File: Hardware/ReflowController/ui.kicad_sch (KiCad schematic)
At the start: 1 part, among them U8 PI4IOE5V6416

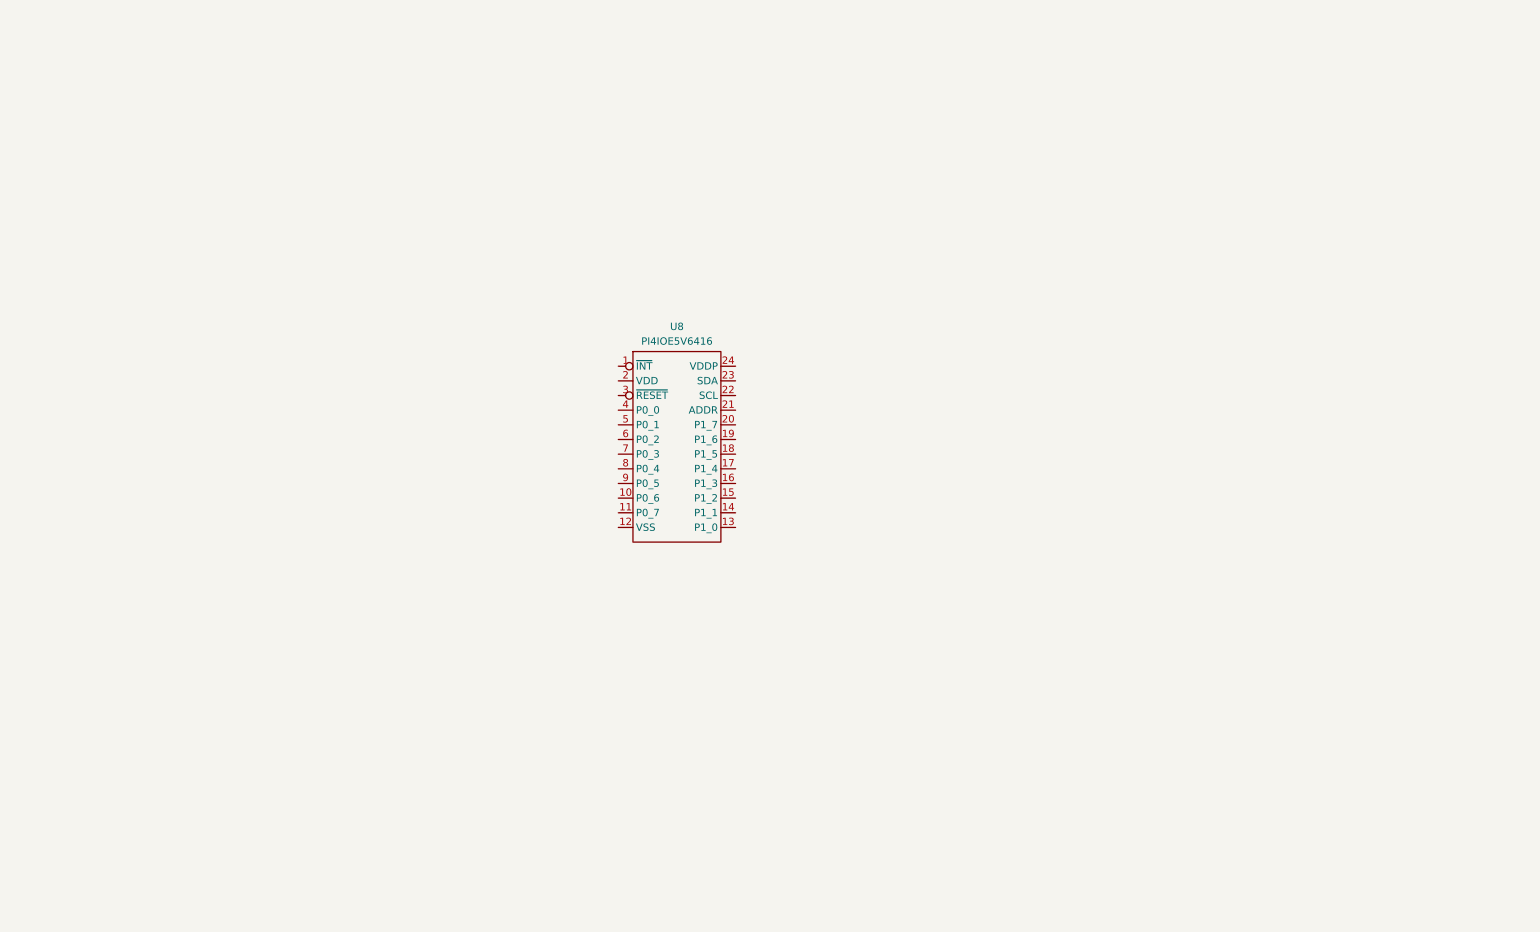
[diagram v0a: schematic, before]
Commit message: added the schematic of the updated pwerAndUi branch(with uC schematic update
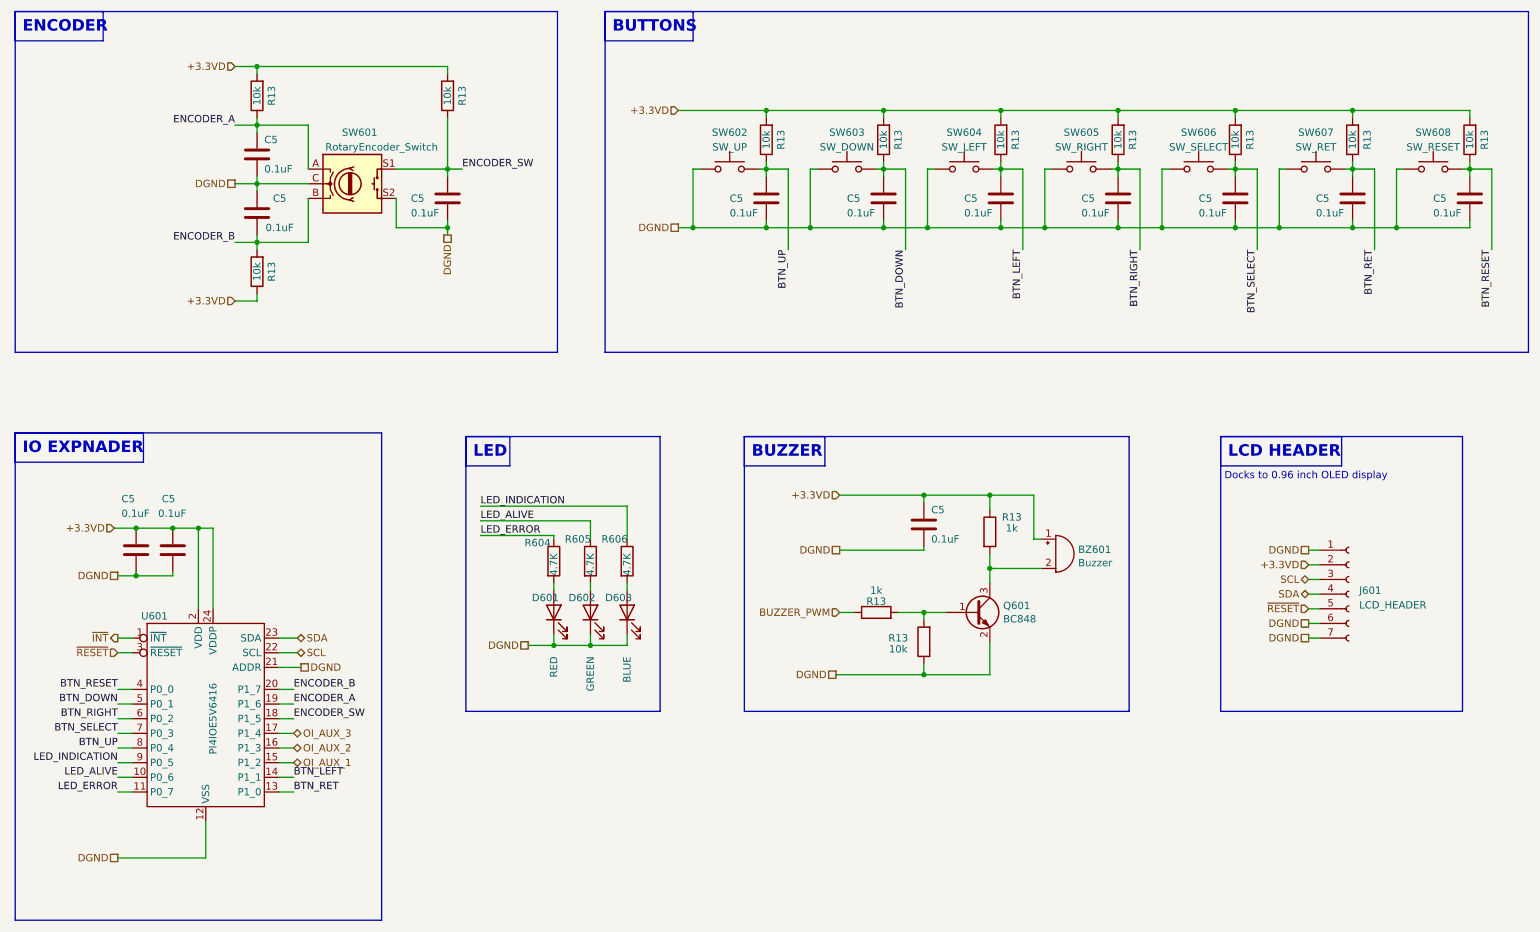
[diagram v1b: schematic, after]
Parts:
- added BZ601: Buzzer, Buzzer_Beeper:Buzzer_TDK_PS1240P02BT_D12.2mm_H6.5mm, symbol Device:Buzzer
- added C5 (x13): 0.1uF, Capacitor_SMD:C_0603_1608Metric_Pad1.08x0.95mm_HandSolder, symbol Device:C
- added D601: RED, LED_SMD:LED_0603_1608Metric_Pad1.05x0.95mm_HandSolder, symbol Device:LED
- added D602: GREEN, LED_SMD:LED_0603_1608Metric_Pad1.05x0.95mm_HandSolder, symbol Device:LED
- added D603: BLUE, LED_SMD:LED_0603_1608Metric_Pad1.05x0.95mm_HandSolder, symbol Device:LED
- added J601: LCD_HEADER, Connector_PinSocket_2.54mm:PinSocket_1x07_P2.54mm_Vertical, symbol Connector:Conn_01x07_Female
- added Q601: BC848, Package_TO_SOT_SMD:SOT-23, symbol Transistor_BJT:BC848
- added R13 (x11): 10k, Resistor_SMD:R_0603_1608Metric_Pad0.98x0.95mm_HandSolder, symbol Device:R
- added R13 (x2): 1k, Resistor_SMD:R_0603_1608Metric_Pad0.98x0.95mm_HandSolder, symbol Device:R
- added R604, R605, R606: 4.7K, Resistor_SMD:R_0603_1608Metric_Pad0.98x0.95mm_HandSolder, symbol Device:R
- added SW601: RotaryEncoder_Switch, Rotary_Encoder:RotaryEncoder_Alps_EC11E-Switch_Vertical_H20mm, symbol Device:RotaryEncoder_Switch
- added SW602: SW_UP, Button_Switch_SMD:SW_SPST_B3S-1000, symbol Switch:SW_Push
- added SW603: SW_DOWN, Button_Switch_SMD:SW_SPST_B3S-1000, symbol Switch:SW_Push
- added SW604: SW_LEFT, Button_Switch_SMD:SW_SPST_B3S-1000, symbol Switch:SW_Push
- added SW605: SW_RIGHT, Button_Switch_SMD:SW_SPST_B3S-1000, symbol Switch:SW_Push
- added SW606: SW_SELECT, Button_Switch_SMD:SW_SPST_B3S-1000, symbol Switch:SW_Push
- added SW607: SW_RET, Button_Switch_SMD:SW_SPST_B3S-1000, symbol Switch:SW_Push
- added SW608: SW_RESET, Button_Switch_SMD:SW_SPST_B3S-1000, symbol Switch:SW_Push
- renumbered U8 to U601
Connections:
- net ~{INT}: now reaches U601.1 (~{INT})
- net LED_ALIVE: now reaches U601.10 (P0_6)
- net LED_ALIVE: now also R605.1
- net LED_ERROR: now reaches U601.11 (P0_7)
- net LED_ERROR: now also R604.1
- net DGND: now reaches U601.12 (VSS)
- net DGND: now also U601.21 (ADDR), C5.2, C5.2, C5.2, C5.2, C5.2, C5.2, C5.2, C5.2, C5.2, C5.2, C5.2, C5.2, C5.2, D601.1 (K), D602.1 (K), D603.1 (K), J601.1 (Pin_1), J601.6 (Pin_6), J601.7 (Pin_7), Q601.2 (E), R13.1, SW601.C, SW601.S2, SW602.1, SW603.1, SW604.1, SW605.1, SW606.1, SW607.1, SW608.1
- net BTN_RET: now reaches U601.13 (P1_0)
- net BTN_RET: now also C5.1, R13.1, SW607.2
- net BTN_LEFT: now reaches U601.14 (P1_1)
- net BTN_LEFT: now also C5.1, R13.1, SW604.2
- net OI_AUX_1: now reaches U601.15 (P1_2)
- net OI_AUX_2: now reaches U601.16 (P1_3)
- net OI_AUX_3: now reaches U601.17 (P1_4)
- net ENCODER_SW: now reaches U601.18 (P1_5)
- net ENCODER_SW: now also C5.1, R13.1, SW601.S1
- net ENCODER_A: now reaches U601.19 (P1_6)
- net ENCODER_A: now also C5.1, R13.1, SW601.A
- net +3.3VD: now reaches U601.2 (VDD)
- net +3.3VD: now also U601.24 (VDDP), BZ601.1 (-), C5.1, C5.1, C5.1, J601.2 (Pin_2), R13.1, R13.1, R13.2, R13.2, R13.2, R13.2, R13.2, R13.2, R13.2, R13.2, R13.2
- net ENCODER_B: now reaches U601.20 (P1_7)
- net ENCODER_B: now also C5.1, R13.2, SW601.B
- net SCL: now reaches U601.22 (SCL)
- net SCL: now also J601.3 (Pin_3)
- net SDA: now reaches U601.23 (SDA)
- net SDA: now also J601.4 (Pin_4)
- net ~{RESET}: now reaches U601.3 (~{RESET})
- net ~{RESET}: now also J601.5 (Pin_5)
- net BTN_RESET: now reaches U601.4 (P0_0)
- net BTN_RESET: now also C5.1, R13.1, SW608.2
- net BTN_DOWN: now reaches U601.5 (P0_1)
- net BTN_DOWN: now also C5.1, R13.1, SW603.2
- net BTN_RIGHT: now reaches U601.6 (P0_2)
- net BTN_RIGHT: now also C5.1, R13.1, SW605.2
- net BTN_SELECT: now reaches U601.7 (P0_3)
- net BTN_SELECT: now also C5.1, R13.1, SW606.2
- net BTN_UP: now reaches U601.8 (P0_4)
- net BTN_UP: now also C5.1, R13.1, SW602.2
- net LED_INDICATION: now reaches U601.9 (P0_5)
- net LED_INDICATION: now also R606.1
- new net: D603.2 (A), R606.2
- new net: D602.2 (A), R605.2
- new net: BZ601.2 (+), Q601.3 (C), R13.2
- new net: Q601.1 (B), R13.2, R13.2
- new net: D601.2 (A), R604.2
- new net BUZZER_PWM: R13.1
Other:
- note added: "BUTTONS"
- note added: "BUZZER"
- note added: "Docks to 0.96 inch OLED display"
- note added: "ENCODER"
- note added: "IO EXPNADER"
- note added: "LCD HEADER"
- note added: "LED"
- moved on the sheet: U601
